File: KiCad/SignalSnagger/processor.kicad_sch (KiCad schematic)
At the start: 57 parts, among them J203 Conn_01x02, J204 Conn_01x02, J205 DB9 Female, P201 ISP/PDI, Q201 BSS84W-7-F, Q202 BSS138W-7-F, SW201 SW_SPST, SW202 SW_SPST, SW203 PEC12R-4225F-S0024, U201 AVR128DA48, U202 SI5351, U205 EA_DOGS104W-A, X202 25 MHz

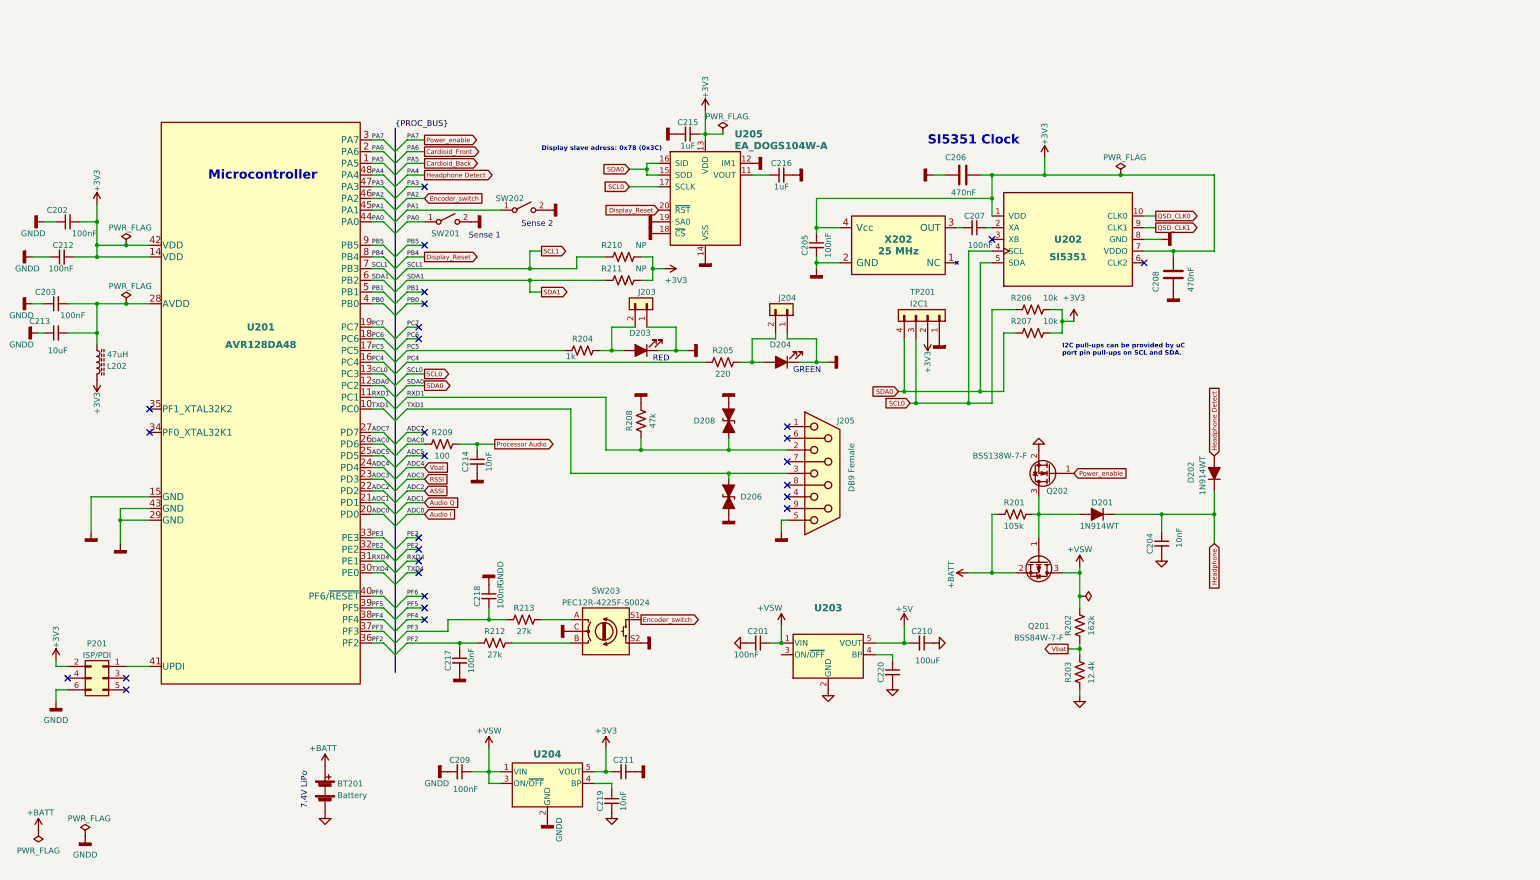
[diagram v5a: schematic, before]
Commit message: Schematic Update
Added +5V processor control
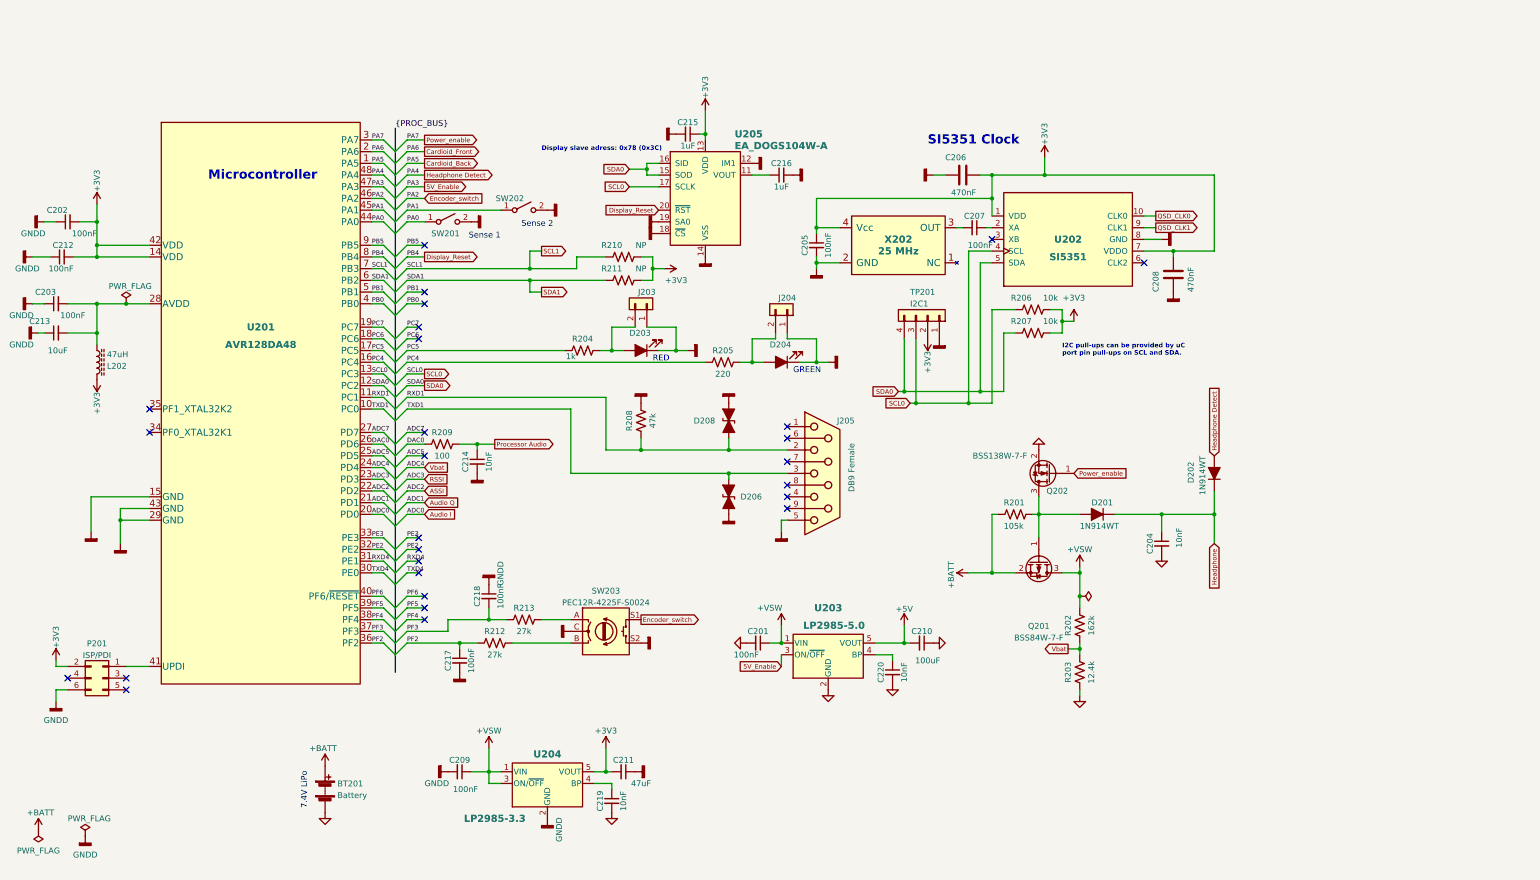
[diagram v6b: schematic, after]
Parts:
- C211: value (none) -> 47uF
- C220: value (none) -> 10nF
- U203: value (none) -> LP2985-5.0; footprint (none) -> Package_TO_SOT_SMD:SOT-23-5
- U204: value (none) -> LP2985-3.3
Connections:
- net PA3 is gone; now on net 5V_Enable: U201.47 (PA3)
- net 5V_Enable: now reaches U203.3 (ON/~{OFF})
- no-connect marks 28 -> 27
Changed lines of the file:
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@@
     (title "SignalSnagger")
     (date "2023-12-19")
-    (rev "0.20")
+    (rev "0.21")
   )
   (bus_alias "PROC_BUS" (members "PA7" "PA6" "PA5" "PA4" "PA3" "PA2" "PA1" "PA0" "PB5" "PB4" "SCL1" "SDA1" "PB1" "PB0" "PC7" "PC6" "PC5" "PC4" "SCL0" "SDA0" "RXD1" "TXD1" "ADC7" "DAC0" "ADC5" "ADC4" "ADC3" "ADC2" "ADC1" "ADC0" "PE3" "PE2" "RXD4" "TXD4" "PF6" "PF5" "PF4" "PF3" "PF2"))
@@
   (junction (at 36.83 123.19) (diameter 0) (color 0 0 0 0)
   )
-  (junction (at 254 48.26) (diameter 0) (color 0 0 0 0)
-  )
   (junction (at 187.96 88.9) (diameter 0) (color 0 0 0 0)
   )
@@
   (junction (at 31.75 58.42) (diameter 0) (color 0 0 0 0)
   )
-  (junction (at 38.1 63.5) (diameter 0) (color 0 0 0 0)
-  )
   (junction (at 151.13 46.99) (diameter 0) (color 0 0 0 0)
   )
@@
   (no_connect (at 102.87 76.2))
   (no_connect (at 43.18 99.06))
-  (no_connect (at 102.87 50.8))
   (no_connect (at 101.6 83.82))
   (no_connect (at 101.6 81.28))
@@
     (stroke (width 0) (type default) (color 0 0 0 0))
   )
-  (wire (pts (xy 254 48.26) (xy 274.32 48.26))
+  (wire (pts (xy 237.49 48.26) (xy 274.32 48.26))
     (stroke (width 0) (type default) (color 0 0 0 0))
   )
@@
     (stroke (width 0) (type default) (color 0 0 0 0))
   )
-  (wire (pts (xy 163.83 39.37) (xy 167.64 39.37))
-    (stroke (width 0) (type default) (color 0 0 0 0))
-  )
   (wire (pts (xy 91.44 50.8) (xy 93.98 50.8))
     (stroke (width 0) (type default) (color 0 0 0 0))
@@
     (stroke (width 0) (type default) (color 0 0 0 0))
   )
-  (wire (pts (xy 31.75 63.5) (xy 38.1 63.5))
+  (wire (pts (xy 31.75 63.5) (xy 43.18 63.5))
     (stroke (width 0) (type default) (color 0 0 0 0))
   )
@@
     (stroke (width 0) (type default) (color 0 0 0 0))
   )
-  (wire (pts (xy 38.1 63.5) (xy 43.18 63.5))
-    (stroke (width 0) (type default) (color 0 0 0 0))
-  )
   (wire (pts (xy 22.86 154.94) (xy 22.86 153.67))
     (stroke (width 0) (type default) (color 0 0 0 0))
@@
     (stroke (width 0) (type default) (color 0 0 0 0))
   )
-  (wire (pts (xy 237.49 48.26) (xy 254 48.26))
-    (stroke (width 0) (type default) (color 0 0 0 0))
-  )
   (wire (pts (xy 31.75 76.2) (xy 38.1 76.2))
     (stroke (width 0) (type default) (color 0 0 0 0))
@@
     (stroke (width 0) (type default) (color 0 0 0 0))
   )
+  (wire (pts (xy 180.34 154.94) (xy 180.34 152.4))
+    (stroke (width 0) (type default) (color 0 0 0 0))
+  )
   (wire (pts (xy 43.18 123.19) (xy 36.83 123.19))
     (stroke (width 0) (type default) (color 0 0 0 0))
@@
     )
   )
+  (global_label "5V_Enable" (shape input) (at 180.34 154.94 180) (fields_autoplaced)
+    (effects (font (size 1 1)) (justify right))
+    (property "Intersheet References" "${INTERSHEET_REFS}" (id 0) (at 170.8686 154.8775 0)
+      (effects (font (size 1 1)) (justify right) hide)
+    )
+  )
+  (global_label "5V_Enable" (shape output) (at 102.87 50.8 0) (fields_autoplaced)
+    (effects (font (size 1 1)) (justify left))
+    (property "Intersheet References" "${INTERSHEET_REFS}" (id 0) (at 112.3414 50.7375 0)
+      (effects (font (size 1 1)) (justify left) hide)
+    )
+  )
   (global_label "Headphone Detect" (shape output) (at 102.87 48.26 0) (fields_autoplaced)
     (effects (font (size 1 1)) (justify left))
@@
       (effects (font (size 1.27 1.27)) hide)
     )
-    (property "Value" "" (id 1) (at 153.67 175.26 90)
+    (property "Value" "GNDD" (id 1) (at 153.67 175.26 90)
       (effects (font (size 1.27 1.27)) (justify left) hide)
     )
@@
       (effects (font (size 1.27 1.27)) hide)
     )
-    (property "Value" "" (id 1) (at 113.03 161.29 90)
+    (property "Value" "GNDD" (id 1) (at 113.03 161.29 90)
       (effects (font (size 1.27 1.27)) (justify left) hide)
     )
@@
       (effects (font (size 1.54 1.54) bold))
     )
-    (property "Value" "" (id 1) (at 191.77 146.05 0)
+    (property "Value" "LP2985-5.0" (id 1) (at 191.77 146.05 0)
       (effects (font (size 1.54 1.54) bold))
     )
-    (property "Footprint" "" (id 2) (at 190.5 144.145 0)
+    (property "Footprint" "Package_TO_SOT_SMD:SOT-23-5" (id 2) (at 190.5 144.145 0)
       (effects (font (size 1.27 1.27)) hide)
     )
@@
     (pin "2")
   )
-  (symbol (lib_id "power:PWR_FLAG") (at 254 48.26 0) (unit 1)
-    (in_bom yes) (on_board yes)
-    (property "Reference" "#FLG0202" (id 0) (at 254 46.355 0)
-      (effects (font (size 1.27 1.27)) hide)
-    )
-    (property "Value" "PWR_FLAG" (id 1) (at 250.19 44.45 0)
-      (effects (font (size 1.27 1.27)) (justify left))
-    )
-    (property "Footprint" "" (id 2) (at 254 48.26 0)
-      (effects (font (size 1.27 1.27)) hide)
-    )
-    (property "Datasheet" "~" (id 3) (at 254 48.26 0)
-      (effects (font (size 1.27 1.27)) hide)
-    )
-    (pin "1")
-  )
   (symbol (lib_id "Device:C_Small") (at 146.05 177.8 270) (unit 1)
     (in_bom yes) (on_board yes)
     (property "Reference" "C211" (id 0) (at 146.05 175.26 90))
-    (property "Value" "" (id 1) (at 149.86 180.34 90))
+    (property "Value" "47uF" (id 1) (at 149.86 180.34 90))
     (property "Footprint" "Capacitor_SMD:C_0805_2012Metric" (id 2) (at 146.05 177.8 0)
       (effects (font (size 1.27 1.27)) hide)
@@
     (pin "2")
   )
-  (symbol (lib_id "power:PWR_FLAG") (at 167.64 39.37 0) (unit 1)
-    (in_bom yes) (on_board yes)
-    (property "Reference" "#FLG0105" (id 0) (at 167.64 37.465 0)
-      (effects (font (size 1.27 1.27)) hide)
-    )
-    (property "Value" "PWR_FLAG" (id 1) (at 163.83 35.56 0)
-      (effects (font (size 1.27 1.27)) (justify left))
-    )
-    (property "Footprint" "" (id 2) (at 167.64 39.37 0)
-      (effects (font (size 1.27 1.27)) hide)
-    )
-    (property "Datasheet" "~" (id 3) (at 167.64 39.37 0)
-      (effects (font (size 1.27 1.27)) hide)
-    )
-    (pin "1")
-  )
   (symbol (lib_id "power:GNDD") (at 107.95 177.8 270) (unit 1)
     (in_bom yes) (on_board yes)
@@
     (pin "1")
   )
-  (symbol (lib_id "power:PWR_FLAG") (at 38.1 63.5 0) (unit 1)
-    (in_bom yes) (on_board yes)
-    (property "Reference" "#FLG0101" (id 0) (at 38.1 61.595 0)
-      (effects (font (size 1.27 1.27)) hide)
-    )
-    (property "Value" "PWR_FLAG" (id 1) (at 34.29 59.69 0)
-      (effects (font (size 1.27 1.27)) (justify left))
-    )
-    (property "Footprint" "" (id 2) (at 38.1 63.5 0)
-      (effects (font (size 1.27 1.27)) hide)
-    )
-    (property "Datasheet" "~" (id 3) (at 38.1 63.5 0)
-      (effects (font (size 1.27 1.27)) hide)
-    )
-    (pin "1")
-  )
   (symbol (lib_id "Device:C_Small") (at 222.25 59.69 270) (unit 1)
     (in_bom yes) (on_board yes)
@@
       (effects (font (size 1.54 1.54) bold))
     )
-    (property "Value" "" (id 1) (at 118.11 187.96 0)
+    (property "Value" "LP2985-3.3" (id 1) (at 118.11 187.96 0)
       (effects (font (size 1.54 1.54) bold))
     )
@@
   (symbol (lib_id "power:GND") (at 245.11 161.29 0) (unit 1)
     (in_bom yes) (on_board yes) (fields_autoplaced)
-    (property "Reference" "#PWR?" (id 0) (at 245.11 167.64 0)
+    (property "Reference" "#PWR0253" (id 0) (at 245.11 167.64 0)
       (effects (font (size 1.27 1.27)) hide)
     )
@@
     (in_bom yes) (on_board yes)
     (property "Reference" "C220" (id 0) (at 201.93 156.21 90))
-    (property "Value" "" (id 1) (at 207.01 156.21 90))
+    (property "Value" "10nF" (id 1) (at 207.01 156.21 90))
     (property "Footprint" "Capacitor_SMD:C_0805_2012Metric" (id 2) (at 204.47 156.21 0)
       (effects (font (size 1.27 1.27)) hide)

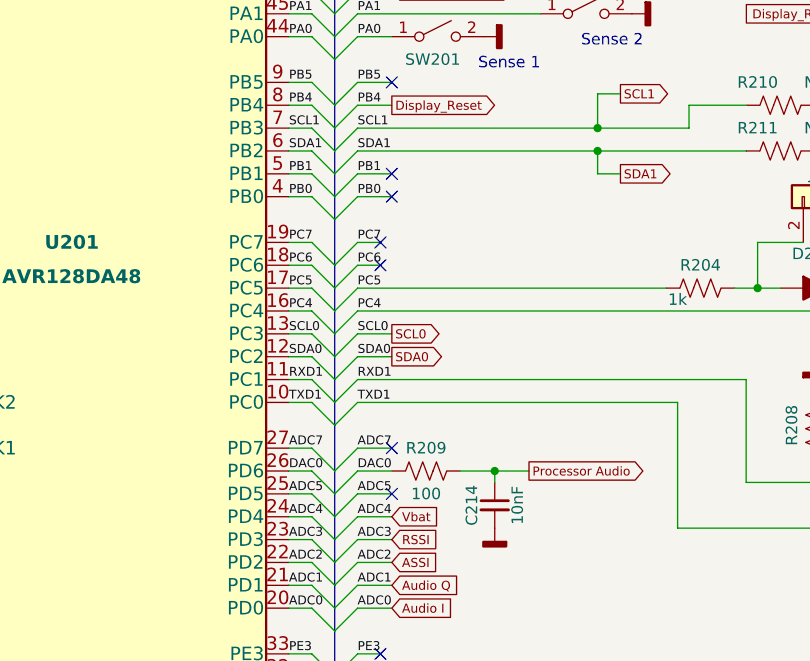
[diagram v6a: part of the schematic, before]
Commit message: Removed Warnings
Trivial changes to remove DRC warnings
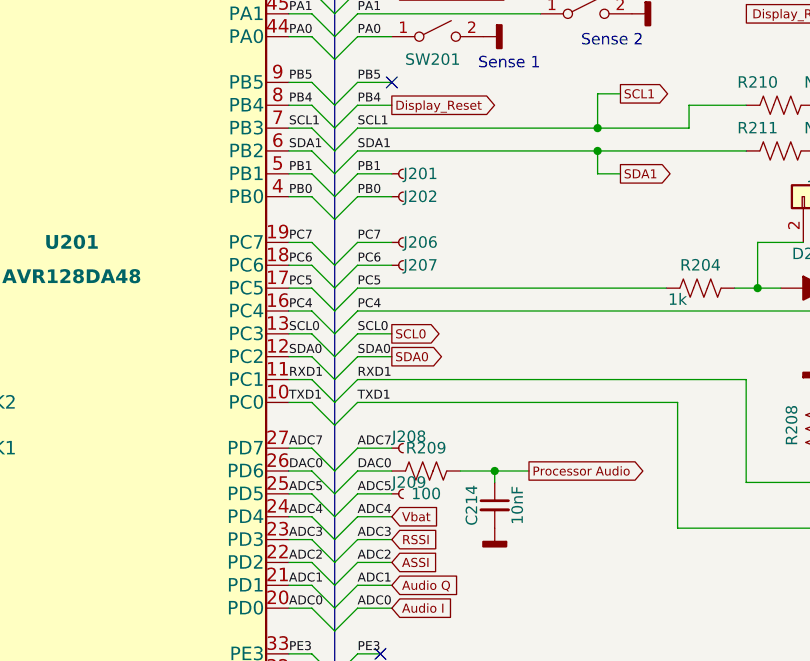
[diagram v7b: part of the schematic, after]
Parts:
- added J201, J202, J206, J207, J208, J209: (no value), symbol Connector:Conn_01x01_Generic
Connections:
- net ADC5: now also J209.1 (Pin_1)
- net ADC7: now also J208.1 (Pin_1)
- net PB0: now also J202.1 (Pin_1)
- net PB1: now also J201.1 (Pin_1)
- net PC6: now also J207.1 (Pin_1)
- net PC7: now also J206.1 (Pin_1)
- no-connect marks 27 -> 21
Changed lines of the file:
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@@
   (no_connect (at 181.61 110.49))
   (no_connect (at 102.87 139.7))
-  (no_connect (at 102.87 109.22))
-  (no_connect (at 102.87 104.14))
   (no_connect (at 102.87 63.5))
-  (no_connect (at 102.87 73.66))
-  (no_connect (at 102.87 76.2))
   (no_connect (at 43.18 99.06))
-  (no_connect (at 101.6 83.82))
-  (no_connect (at 101.6 81.28))
   (no_connect (at 102.87 142.24))
   (no_connect (at 38.1 160.02))
@@
     (stroke (width 0) (type default) (color 0 0 0 0))
   )
-  (wire (pts (xy 99.06 81.28) (xy 101.6 81.28))
+  (wire (pts (xy 99.06 81.28) (xy 102.87 81.28))
     (stroke (width 0) (type default) (color 0 0 0 0))
   )
@@
     (stroke (width 0) (type default) (color 0 0 0 0))
   )
-  (wire (pts (xy 99.06 83.82) (xy 101.6 83.82))
+  (wire (pts (xy 99.06 83.82) (xy 102.87 83.82))
     (stroke (width 0) (type default) (color 0 0 0 0))
   )
@@
     )
   )
+  (symbol (lib_id "Connector:Conn_01x01_Generic") (at 104.14 76.2 0) (unit 1)
+    (in_bom yes) (on_board yes)
+    (property "Reference" "J202" (id 0) (at 104.14 76.2 0)
+      (effects (font (size 1.27 1.27)) (justify left))
+    )
+    (property "Value" "" (id 1) (at 104.8512 77.9022 0)
+      (effects (font (size 1.27 1.27)) (justify left) hide)
+    )
+    (property "Footprint" "" (id 2) (at 104.14 76.2 0)
+      (effects (font (size 1.27 1.27)) hide)
+    )
+    (property "Datasheet" "~" (id 3) (at 104.14 76.2 0)
+      (effects (font (size 1.27 1.27)) hide)
+    )
+    (pin "1")
+  )
   (symbol (lib_id "Device:R_Small_US") (at 137.16 86.36 90) (unit 1)
     (in_bom yes) (on_board yes)
@@
     (pin "2")
   )
+  (symbol (lib_id "Connector:Conn_01x01_Generic") (at 104.14 81.28 0) (unit 1)
+    (in_bom yes) (on_board yes)
+    (property "Reference" "J206" (id 0) (at 104.14 81.28 0)
+      (effects (font (size 1.27 1.27)) (justify left))
+    )
+    (property "Value" "" (id 1) (at 104.8512 82.9822 0)
+      (effects (font (size 1.27 1.27)) (justify left) hide)
+    )
+    (property "Footprint" "" (id 2) (at 104.14 81.28 0)
+      (effects (font (size 1.27 1.27)) hide)
+    )
+    (property "Datasheet" "~" (id 3) (at 104.14 81.28 0)
+      (effects (font (size 1.27 1.27)) hide)
+    )
+    (pin "1")
+  )
   (symbol (lib_id "Device:C_Small") (at 22.86 76.2 90) (mirror x) (unit 1)
     (in_bom yes) (on_board yes)
@@
     (pin "S2")
   )
+  (symbol (lib_id "Connector:Conn_01x01_Generic") (at 104.14 104.14 0) (unit 1)
+    (in_bom yes) (on_board yes)
+    (property "Reference" "J208" (id 0) (at 102.87 102.87 0)
+      (effects (font (size 1.27 1.27)) (justify left))
+    )
+    (property "Value" "" (id 1) (at 104.8512 105.8422 0)
+      (effects (font (size 1.27 1.27)) (justify left) hide)
+    )
+    (property "Footprint" "" (id 2) (at 104.14 104.14 0)
+      (effects (font (size 1.27 1.27)) hide)
+    )
+    (property "Datasheet" "~" (id 3) (at 104.14 104.14 0)
+      (effects (font (size 1.27 1.27)) hide)
+    )
+    (pin "1")
+  )
   (symbol (lib_id "power:PWR_FLAG") (at 38.1 76.2 0) (unit 1)
     (in_bom yes) (on_board yes)
@@
     (pin "2")
   )
+  (symbol (lib_id "Connector:Conn_01x01_Generic") (at 104.14 73.66 0) (unit 1)
+    (in_bom yes) (on_board yes)
+    (property "Reference" "J201" (id 0) (at 104.14 73.66 0)
+      (effects (font (size 1.27 1.27)) (justify left))
+    )
+    (property "Value" "" (id 1) (at 104.8512 75.3622 0)
+      (effects (font (size 1.27 1.27)) (justify left) hide)
+    )
+    (property "Footprint" "" (id 2) (at 104.14 73.66 0)
+      (effects (font (size 1.27 1.27)) hide)
+    )
+    (property "Datasheet" "~" (id 3) (at 104.14 73.66 0)
+      (effects (font (size 1.27 1.27)) hide)
+    )
+    (pin "1")
+  )
   (symbol (lib_id "power:GNDD") (at 160.02 86.36 90) (mirror x) (unit 1)
     (in_bom yes) (on_board yes)
@@
     (pin "2")
   )
+  (symbol (lib_id "Connector:Conn_01x01_Generic") (at 104.14 83.82 0) (unit 1)
+    (in_bom yes) (on_board yes)
+    (property "Reference" "J207" (id 0) (at 104.14 83.82 0)
+      (effects (font (size 1.27 1.27)) (justify left))
+    )
+    (property "Value" "" (id 1) (at 104.8512 85.5222 0)
+      (effects (font (size 1.27 1.27)) (justify left) hide)
+    )
+    (property "Footprint" "" (id 2) (at 104.14 83.82 0)
+      (effects (font (size 1.27 1.27)) hide)
+    )
+    (property "Datasheet" "~" (id 3) (at 104.14 83.82 0)
+      (effects (font (size 1.27 1.27)) hide)
+    )
+    (pin "1")
+  )
   (symbol (lib_id "power:GNDD") (at 157.48 39.37 270) (unit 1)
     (in_bom yes) (on_board yes)
@@
       (effects (font (size 1.27 1.27)) hide)
     )
+    (pin "1")
+  )
+  (symbol (lib_id "Connector:Conn_01x01_Generic") (at 104.14 109.22 0) (unit 1)
+    (in_bom yes) (on_board yes)
+    (property "Reference" "J209" (id 0) (at 102.87 107.95 0)
+      (effects (font (size 1.27 1.27)) (justify left))
+    )
+    (property "Value" "" (id 1) (at 104.8512 110.9222 0)
+      (effects (font (size 1.27 1.27)) (justify left) hide)
+    )
+    (property "Footprint" "" (id 2) (at 104.14 109.22 0)
+      (effects (font (size 1.27 1.27)) hide)
+    )
+    (property "Datasheet" "~" (id 3) (at 104.14 109.22 0)
+      (effects (font (size 1.27 1.27)) hide)
+    )

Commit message: Ver 0.22
o Schematic updates
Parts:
- added R214: (no value), Resistor_SMD:R_0805_2012Metric, symbol Device:R_Small_US
- added R215: 10k, Resistor_SMD:R_0805_2012Metric, symbol Device:R_Small_US
- J201, J202, J206, J207, J208, J209: value (none) -> Conn_01x01_Female
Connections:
- net +3V3: now also R215.2
- net GND: now also R214.2
- net Headphone Detect: now also R215.1
- net Power_enable: now also R214.1
- net ASSI renamed ASSI_NEAR
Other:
- note added: "Remove R215 if testing proves this pull-up is unneeded"
